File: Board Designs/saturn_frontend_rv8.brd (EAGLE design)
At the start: 29 x 23.8 mm, 26 parts

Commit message: Both Boards mocked up, both need testing
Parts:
- removed E$1: (no value), cody_custom_library:ATB2012E-50011M-T01
- removed U54: (no value), SOP65P490X110-8N:SOP65P490X110-8N
- added E$2: (no value), cody_custom_library:SKY13431-374LF
- added T1: (no value), cody_custom_library:BALH-0006SMG
- moved C855 0.18 mm to (36.3, 38.9)
- moved RX1_AUX 0.18 mm to (17.5, 23.9)
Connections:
- net S$16 renamed S$36
- net S$19 renamed S$37
- removed net S$10: C750.1, R474.2, U54.2
- removed net S$28: E$1.1, R17.1, R25.1
- removed net S$29: C953.2, E$1.3, L26.1
- removed net S$5: C860.1, U54.8
- new net S$23: C859.2, PAD4.1
- new net S$24: C953.2, L26.1, T1.P$2
- new net S$32: C860.2, RX1_AUX.3
- new net S$34: R17.2, T1.P$1
- new net S$38: C855.2, RX1_P.1
- new net S$39: C856.2, RX1_N.1
- net GND: now also E$2.P$5; no longer E$1.2, U54.6, U54.7
- net S$1: now also C751.1, E$2.P$1, R473.2; no longer C859.2, PAD4.1
- net S$12: now also E$2.P$2; no longer U54.3
- net S$18: now also T1.P$3; no longer E$1.4
- net S$2: now also C750.1, E$2.P$3, R474.2; no longer C860.2, RX1_AUX.3
- net S$25: now also C859.1, E$2.P$4; no longer C855.2, RX1_P.1
- net S$27: now also C860.1, E$2.P$6; no longer C856.2, RX1_N.1
- net S$3: now also T1.P$4; no longer C859.1, U54.5
- net S$8: now also R17.1, R25.1; no longer C751.1, R473.2, U54.1
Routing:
- net GND: track 4.86 -> 73.9 mm, vias 0 -> 4
- net S$10: track 18.3 -> 0.00 mm
- net S$8: track 13.4 -> 1.21 mm
- net S$2: track 9.56 -> 21.0 mm, vias 0 -> 2
- net S$32: track 0.00 -> 9.95 mm
- net S$1: track 4.63 -> 13.6 mm
- net S$28: track 7.38 -> 0.00 mm
- net S$23: track 0.00 -> 4.63 mm
- net S$34: track 0.00 -> 4.41 mm
- net S$24: track 0.00 -> 4.26 mm
- net S$29: track 3.19 -> 0.00 mm
- net S$3: track 3.61 -> 0.61 mm
- net S$39: track 0.00 -> 2.51 mm
- net S$38: track 0.00 -> 2.42 mm
- net S$25: track 2.82 -> 5.11 mm
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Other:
- board text removed: "Rx"
- board text removed: "T1"

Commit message: Fixed the component size in library and in layout
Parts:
- removed T1: (no value), cody_custom_library:BALH-0006SMG
- added E$1: (no value), cody_custom_library:BALH-0006SMG
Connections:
- removed net S$3: T1.P$4
- removed net S$34: R17.2, T1.P$1
- net GND: now also E$1.GND, R17.2
- net S$18: now also E$1.2; no longer T1.P$3
- net S$24: now also E$1.3; no longer T1.P$2
- net S$8: now also E$1.1
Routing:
- net S$8: track 1.21 -> 17.4 mm
- net GND: track 73.9 -> 83.8 mm
- net S$34: track 4.41 -> 0.00 mm
- net S$24: track 4.26 -> 6.79 mm
- net S$18: track 4.36 -> 5.44 mm
- net S$3: track 0.61 -> 0.00 mm
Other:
- board size 29 x 23.8 mm -> 31.6 x 25.1 mm
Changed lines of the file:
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@@
 <board>
 <plain>
-<wire x1="40.7162" y1="43.3832" x2="40.7162" y2="19.558" width="0.4064" layer="20"/>
-<wire x1="40.7162" y1="19.558" x2="11.7348" y2="19.558" width="0.4064" layer="20"/>
-<wire x1="11.7348" y1="19.558" x2="11.7348" y2="43.3832" width="0.4064" layer="20"/>
-<wire x1="40.7162" y1="43.3832" x2="11.7348" y2="43.3832" width="0.4064" layer="20"/>
+<wire x1="43.3832" y1="44.6532" x2="43.3832" y2="19.558" width="0.4064" layer="20"/>
+<wire x1="43.3832" y1="19.558" x2="11.7348" y2="19.558" width="0.4064" layer="20"/>
+<wire x1="11.7348" y1="19.558" x2="11.7348" y2="44.6532" width="0.4064" layer="20"/>
+<wire x1="43.3832" y1="44.6532" x2="11.7348" y2="44.6532" width="0.4064" layer="20"/>
 <text x="14.9352" y="26.1366" size="0.65" layer="21" ratio="16">Tx</text>
 <text x="15.113" y="21.336" size="0.65" layer="21" ratio="16">P</text>
@@
 </element>
 <element name="RX1_P" library="adafruit" package="1X01" value="" x="36.5506" y="41.91" smashed="yes">
-<attribute name="NAME" x="35.0266" y="43.0276" size="0.65" layer="25" ratio="10" rot="R180"/>
+<attribute name="NAME" x="37.1602" y="44.0944" size="0.65" layer="25" ratio="10" rot="R180"/>
 <attribute name="VALUE" x="35.2806" y="38.735" size="1.27" layer="27"/>
 </element>
 <element name="RX1_N" library="adafruit" package="1X01" value="" x="39.1414" y="41.91" smashed="yes">
-<attribute name="NAME" x="32.4612" y="41.4274" size="0.65" layer="25" ratio="10"/>
+<attribute name="NAME" x="37.7952" y="43.561" size="0.65" layer="25" ratio="10"/>
 <attribute name="VALUE" x="37.8714" y="38.735" size="1.27" layer="27"/>
 </element>
@@
 </element>
 <element name="C856" library="eagle-ltspice" package="C0402" value="100 pF" x="38.6842" y="38.9382" smashed="yes" rot="R90">
-<attribute name="NAME" x="40.005" y="38.3032" size="0.65" layer="25" rot="R90"/>
-<attribute name="VALUE" x="37.9222" y="38.3032" size="0.65" layer="27" rot="R90"/>
+<attribute name="NAME" x="40.3606" y="37.9476" size="0.65" layer="25" rot="R90"/>
+<attribute name="VALUE" x="41.3004" y="37.592" size="0.65" layer="27" rot="R90"/>
 </element>
 <element name="PAD1" library="project_1" package="PAD_0PRIMARY" value="" x="14.3523" y="40.1535" smashed="yes" rot="MR270">
@@
 <attribute name="VALUE" x="37.719" y="34.29" size="0.65" layer="27" rot="R90"/>
 </element>
-<element name="T1" library="cody_custom_library" package="BALH-0006SMG" value="" x="37.8714" y="30.9372" smashed="yes" rot="R180"/>
 <element name="E$2" library="cody_custom_library" package="SKY13431-374LF" value="" x="26.4922" y="35.9156" smashed="yes" rot="R180"/>
+<element name="E$1" library="cody_custom_library" package="BALH-0006SMG" value="" x="40.7162" y="29.6926" rot="R180"/>
 </elements>
 <signals>
@@
 <wire x1="32.2834" y1="31.5318" x2="32.2834" y2="30.338" width="0.4064" layer="1"/>
 <wire x1="32.2834" y1="30.338" x2="32.2938" y2="30.3276" width="0.4064" layer="1"/>
+<contactref element="E$1" pad="1"/>
+<wire x1="32.2938" y1="30.3276" x2="31.2166" y2="30.3276" width="0.4064" layer="1"/>
+<wire x1="31.2166" y1="30.3276" x2="30.7594" y2="29.8704" width="0.4064" layer="1"/>
+<wire x1="30.7594" y1="29.8704" x2="30.7594" y2="21.5138" width="0.4064" layer="1"/>
+<wire x1="30.7594" y1="21.5138" x2="31.6484" y2="20.6248" width="0.4064" layer="1"/>
+<wire x1="31.6484" y1="20.6248" x2="36.3484" y2="20.6248" width="0.4064" layer="1"/>
+<wire x1="36.3484" y1="20.6248" x2="36.4662" y2="20.7426" width="0.4064" layer="1"/>
 </signal>
 <signal name="S$24">
@@
 <wire x1="36.8658" y1="33.1216" x2="36.7538" y2="33.1216" width="0.4064" layer="1"/>
 <wire x1="36.9824" y1="33.005" x2="36.8658" y2="33.1216" width="0.4064" layer="1"/>
-<contactref element="T1" pad="P$2"/>
 <contactref element="L26" pad="1"/>
 <wire x1="36.2712" y1="34.3766" x2="36.3474" y2="34.4528" width="0.4064" layer="1"/>
-<wire x1="37.6514" y1="30.9522" x2="37.6514" y2="31.335" width="0.0254" layer="1"/>
-<wire x1="37.6514" y1="31.335" x2="36.9824" y2="32.004" width="0.0254" layer="1"/>
-<wire x1="36.9824" y1="32.004" x2="36.9824" y2="33.005" width="0.0254" layer="1"/>
 <wire x1="36.3474" y1="34.4528" x2="36.3474" y2="33.64" width="0.4064" layer="1"/>
 <wire x1="36.3474" y1="33.64" x2="36.8658" y2="33.1216" width="0.4064" layer="1"/>
+<contactref element="E$1" pad="3"/>
+<wire x1="35.0662" y1="29.8426" x2="35.0662" y2="30.799" width="0.4064" layer="1"/>
+<wire x1="35.0662" y1="30.799" x2="35.3822" y2="31.115" width="0.4064" layer="1"/>
+<wire x1="35.3822" y1="31.115" x2="36.8046" y2="31.115" width="0.4064" layer="1"/>
+<wire x1="36.8046" y1="31.115" x2="36.8046" y2="33.0604" width="0.4064" layer="1"/>
+<wire x1="36.8046" y1="33.0604" x2="36.8658" y2="33.1216" width="0.4064" layer="1"/>
 </signal>
 <signal name="S$18">
@@
 <wire x1="38.2448" y1="33.0426" x2="38.1658" y2="33.1216" width="0.4064" layer="1"/>
 <wire x1="38.1658" y1="33.1216" x2="38.1658" y2="33.1874" width="0.4064" layer="1"/>
-<contactref element="T1" pad="P$3"/>
 <contactref element="L27" pad="1"/>
 <wire x1="38.5826" y1="34.3766" x2="38.6588" y2="34.4528" width="0.4064" layer="1"/>
-<wire x1="37.7614" y1="30.9522" x2="37.7614" y2="31.3606" width="0.0254" layer="1"/>
-<wire x1="37.7614" y1="31.3606" x2="38.227" y2="31.8262" width="0.0254" layer="1"/>
-<wire x1="38.227" y1="31.8262" x2="38.227" y2="33.0604" width="0.0254" layer="1"/>
-<wire x1="38.227" y1="33.0604" x2="38.1658" y2="33.1216" width="0.0254" layer="1"/>
 <wire x1="38.1658" y1="33.1216" x2="38.2778" y2="33.1216" width="0.4064" layer="1"/>
 <wire x1="38.2778" y1="33.1216" x2="38.7604" y2="33.6042" width="0.4064" layer="1"/>
 <wire x1="38.7604" y1="33.6042" x2="38.7604" y2="34.3512" width="0.4064" layer="1"/>
 <wire x1="38.7604" y1="34.3512" x2="38.6588" y2="34.4528" width="0.4064" layer="1"/>
+<contactref element="E$1" pad="2"/>
+<wire x1="37.8162" y1="29.8426" x2="37.8162" y2="30.7042" width="0.4064" layer="1"/>
+<wire x1="37.8162" y1="30.7042" x2="38.227" y2="31.115" width="0.4064" layer="1"/>
+<wire x1="38.227" y1="31.115" x2="38.227" y2="33.0604" width="0.4064" layer="1"/>
+<wire x1="38.227" y1="33.0604" x2="38.1658" y2="33.1216" width="0.4064" layer="1"/>
 </signal>
 <signal name="S$3">
-<contactref element="T1" pad="P$4"/>
-<wire x1="37.7064" y1="30.7772" x2="37.3202" y2="30.7772" width="0.0254" layer="1"/>
-<wire x1="37.3202" y1="30.7772" x2="37.1602" y2="30.9372" width="0.0254" layer="1"/>
 </signal>
 <signal name="GND">
@@
 <wire x1="14.224" y1="38.5826" x2="14.224" y2="29.5148" width="0.254" layer="16"/>
 <wire x1="14.4018" y1="38.5826" x2="14.4018" y2="39.4716" width="0.254" layer="16"/>
+<contactref element="R17" pad="2"/>
+<wire x1="33.6954" y1="30.226" x2="33.5938" y2="30.3276" width="0.0254" layer="1"/>
+<wire x1="33.5938" y1="30.3276" x2="33.5938" y2="33.9852" width="0.4064" layer="1"/>
+<wire x1="33.5938" y1="33.9852" x2="33.5684" y2="34.0106" width="0.4064" layer="1"/>
+<contactref element="E$1" pad="GND"/>
+<wire x1="33.6954" y1="30.226" x2="33.6954" y2="28.0634" width="0.4064" layer="1"/>
+<wire x1="33.6954" y1="28.0634" x2="36.4662" y2="25.2926" width="0.4064" layer="1"/>
 </signal>
 <signal name="S$16">
@@
 <wire x1="21.6916" y1="32.4208" x2="21.7424" y2="32.4716" width="0.4064" layer="1"/>
 </signal>
-<signal name="S$34">
-<contactref element="T1" pad="P$1"/>
-<contactref element="R17" pad="2"/>
-<wire x1="37.7064" y1="30.5922" x2="37.7064" y2="30.4166" width="0.0254" layer="1"/>
-<wire x1="37.7064" y1="30.4166" x2="37.5158" y2="30.226" width="0.0254" layer="1"/>
-<wire x1="37.5158" y1="30.226" x2="33.6954" y2="30.226" width="0.4064" layer="1"/>
-<wire x1="33.6954" y1="30.226" x2="33.5938" y2="30.3276" width="0.0254" layer="1"/>
-</signal>
 <signal name="S$36">

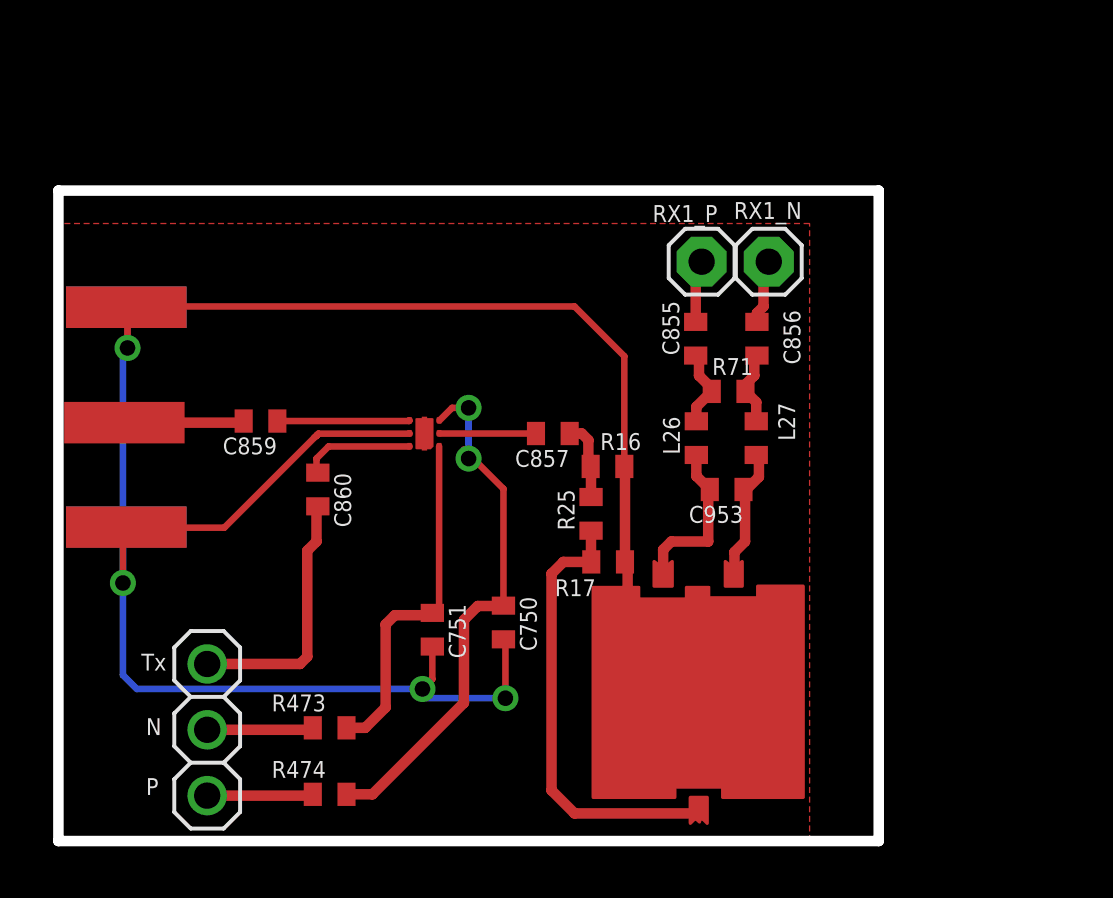
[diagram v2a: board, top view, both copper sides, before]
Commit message: added some scpi commands
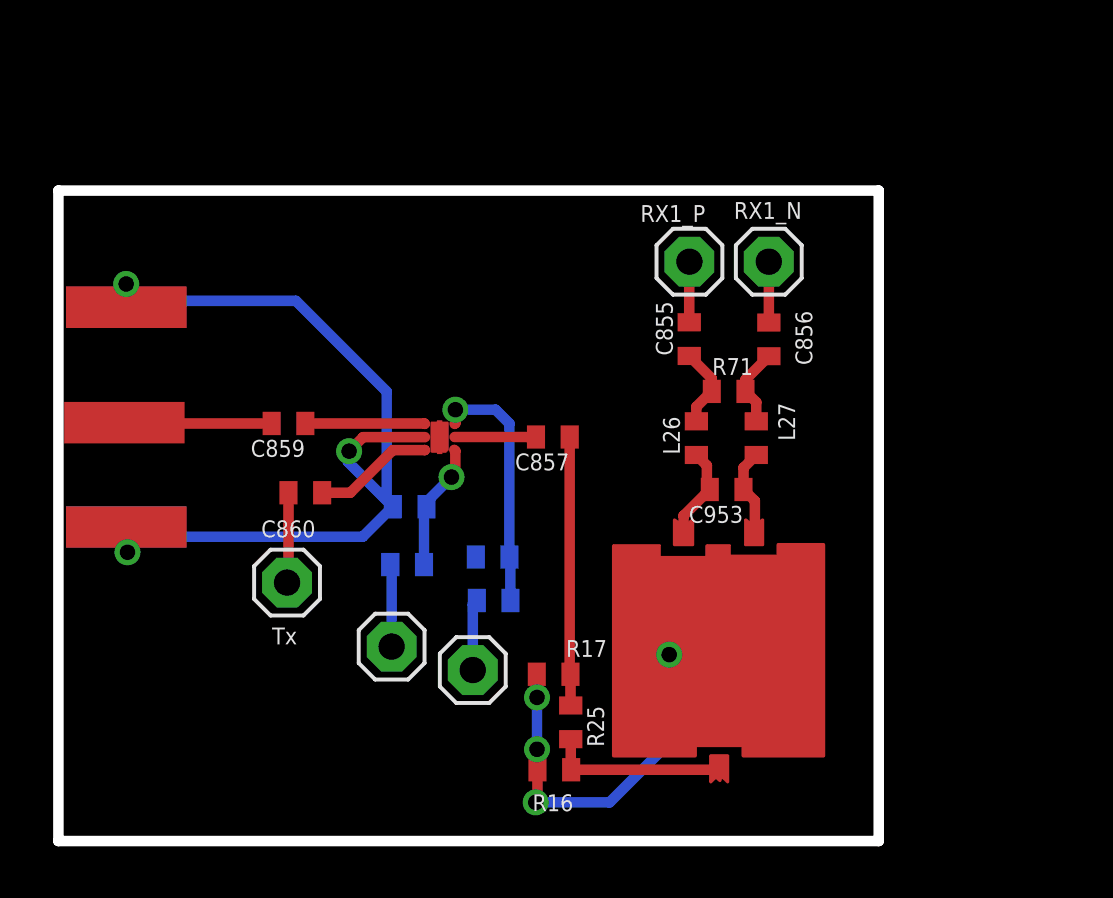
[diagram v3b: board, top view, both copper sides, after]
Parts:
- removed RX1_AUX: (no value), adafruit:1X03
- added RX1_N1, RX1_N2, RX1_P1: (no value), adafruit:1X01
- moved R16 11.9 mm to (30.9, 22.3), turned to 180 degrees
- moved R474 9.79 mm to (28.5, 28.8), flipped to the bottom, turned to 180 degrees
- moved R25 8.08 mm to (31.5, 24.1), turned to 270 degrees
- moved R473 6.97 mm to (25.2, 30.2), flipped to the bottom, turned to 180 degrees
- moved C751 4.83 mm to (25.3, 32.5), flipped to the bottom, turned to 0 degrees
- moved R17 4.82 mm to (30.8, 26.0), turned to 180 degrees
- moved C750 2.56 mm to (28.5, 30.5), flipped to the bottom, turned to 0 degrees
- moved E$1 1.79 mm to (41.5, 31.3)
- moved C859 1.08 mm to (20.6, 35.7)
- moved E$2 0.60 mm to (27.1, 35.8)
- moved C860 0.50 mm to (21.3, 33.0), turned to 180 degrees
- moved RX1_P 0.47 mm to (36.1, 41.9)
- moved C856 0.46 mm to (39.1, 38.9)
- moved C855 0.25 mm to (36.1, 38.9)
- moved C857 0.13 mm to (30.8, 35.1)
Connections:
- net S$36 renamed S$33
- removed net S$14: C857.1, R16.1, R25.2
- removed net S$7: R474.1, RX1_AUX.1
- new net S$10: E$1.1, R16.1, R25.2
- new net S$28: C750.2
- new net S$34: C856.1, L27.2, R71.2
- net GND: no longer C750.2
- net S$32: now also RX1_P1.1; no longer RX1_AUX.3
- net S$37: now also R474.1, RX1_N2.1; no longer C856.1, L27.2, R71.2
- net S$6: now also RX1_N1.1; no longer RX1_AUX.2
- net S$8: now also C857.1; no longer E$1.1
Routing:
- net GND: track 83.8 -> 52.7 mm, vias 4 -> 7
- net S$2: track 21.0 -> 9.71 mm, vias 2 -> 1
- net S$1: track 13.6 -> 4.95 mm, vias 0 -> 1
- net S$8: track 17.4 -> 10.4 mm
- net S$10: track 0.00 -> 6.94 mm
- net S$32: track 9.95 -> 3.49 mm
- net S$7: track 4.10 -> 0.00 mm
- net S$14: track 3.21 -> 0.00 mm
- net S$34: track 0.00 -> 3.06 mm
- net S$24: track 6.79 -> 4.07 mm
- net S$18: track 5.44 -> 3.50 mm
- net S$23: track 4.63 -> 5.69 mm
- net S$6: track 4.11 -> 3.18 mm
- net S$12: track 3.91 -> 3.27 mm
- added copper zone on layer 16, net GND
- removed copper zone on layer 1, net GND

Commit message: Another Revision of the boards, with more sma connectors
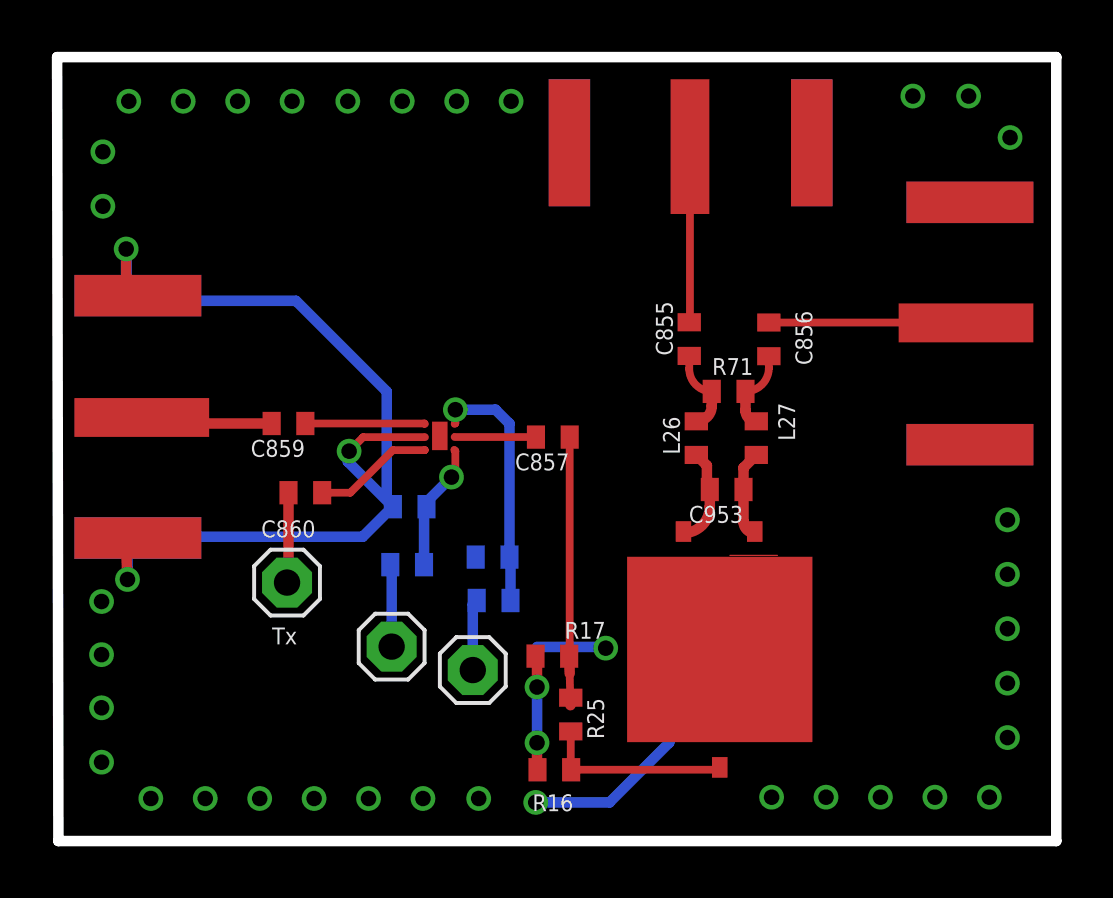
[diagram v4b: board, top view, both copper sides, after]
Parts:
- removed PAD1, PAD2, PAD4, PAD8113, PAD8114: (no value), project_1:PAD_0PRIMARY
- removed RX1_N, RX1_P: (no value), adafruit:1X01
- added E$3, E$4, E$5: (no value), cody_custom_library:SMA132289
- moved E$2 1.77 mm to (25.8, 34.5), turned to 0 degrees
- moved R17 0.70 mm to (30.8, 26.7)
- moved R25 0.30 mm to (31.5, 24.4)
- moved E$1 0.06 mm to (41.5, 31.4)
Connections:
- net S$33 renamed S$43
- net S$34 renamed S$44
- removed net S$18: C953.1, E$1.2, L27.1
- removed net S$23: C859.2, PAD4.1
- removed net S$39: C856.2, RX1_N.1
- new net S$40: C953.1, L27.1
- new net S$5: C855.2, E$5.P$3
- new net S$79: C859.2, E$3.P$3
- net GND: now also E$3.GND, E$3.P$5, E$4.GND, E$4.P$5, E$5.GND, E$5.P$5; no longer E$2.P$5, PAD8113.1, PAD8114.1
- net S$1: no longer E$2.P$1
- net S$10: no longer E$1.1
- net S$12: no longer E$2.P$2
- net S$2: no longer E$2.P$3
- net S$24: no longer E$1.3
- net S$25: no longer E$2.P$4
- net S$27: no longer E$2.P$6
- net S$38: now also C856.2, E$4.P$3; no longer C855.2, RX1_P.1
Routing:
- net S$5: track 0.00 -> 6.80 mm
- net GND: track 52.7 -> 59.0 mm
- net S$23: track 5.69 -> 0.00 mm
- net S$38: track 2.34 -> 7.62 mm
- net S$79: track 0.00 -> 5.24 mm
- net S$40: track 0.00 -> 3.50 mm
- net S$18: track 3.50 -> 0.00 mm
- net S$39: track 2.35 -> 0.00 mm, vias 0 -> 1
- net S$8: track 10.4 -> 12.0 mm
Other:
- board size 31.6 x 25.1 mm -> 38.5 x 30.2 mm

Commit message: Next Revision of board
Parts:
- removed E$1: (no value), cody_custom_library:BALH-0006SMG
- added E$6: (no value), cody_custom_library:BALH-0006SMG
- moved C856 0.30 mm to (39.1, 39.2)
- moved R71 0.21 mm to (37.6, 37.1)
- moved C855 0.20 mm to (36.1, 39.1)
- moved C953 0.15 mm to (37.5, 33.0)
- moved L26 0.05 mm to (36.3, 35.1)
- moved L27 0.05 mm to (38.7, 35.1)
- moved R17 0.05 mm to (30.8, 26.7)
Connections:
- removed net S$8: C857.1, R17.1, R25.1
- new net S$81: R25.1
- net GND: now also E$4.P$1, E$4.P$2, E$5.P$1, E$5.P$2, E$6.GND; no longer E$1.GND
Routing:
- net S$8: track 12.0 -> 0.00 mm, vias 0 -> 1
- net GND: track 59.0 -> 70.3 mm, vias 7 -> 10
- added copper zone on layer 1, net SIGGND
